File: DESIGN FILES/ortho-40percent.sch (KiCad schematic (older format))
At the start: 28 parts, among them J1 USB-C_Receptacle-24, SW1 SW_NO_4-Pin, U1 U_TPD4E05U06DQAR, U2 U_ATmega32u4-MU, Y1 XTAL_4Lead

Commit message: Consolidating design files
Added directory to store design separate from production files
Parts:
- removed C1, C2: C, ortho-40percent:C_0805, symbol master-vampire_General:C
- added C1, C2: C, master-vampire:C_0805, symbol master-vampire:C
- J1: symbol master-vampire_General:USB-C_Receptacle-24 -> master-vampire:USB-C_Receptacle-24
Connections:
- wire segments 171 -> 175
- no-connect marks 10 -> 13
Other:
- note added: "B"
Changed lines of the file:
@@
 $EndDescr
 $Comp
-L master-vampire_General:USB-C_Receptacle-24 J1
+L master-vampire:USB-C_Receptacle-24 J1
 U 1 1 5F1E69AB
 P 1450 2200
@@
 $EndComp
 $Comp
-L master-vampire_General:C C1
-U 1 1 5F248795
-P 5900 3650
-F 0 "C1" H 6015 3703 50  0000 L CNN
-F 1 "C" H 5900 3900 50  0001 L CNN
-F 2 "ortho-40percent:C_0805" H 5300 3450 50  0001 C CNN
-F 3 "" H 6050 3750 50  0000 C CNN
-F 4 "22pF" H 6015 3604 60  0000 L CNN "Capacitance"
-F 5 "50V" H 6400 3550 60  0001 C CNN "Voltage Rating"
-F 6 "C0G/NP0" H 6200 3500 60  0000 C CNN "TempCo"
-F 7 "±5%" H 6450 3650 60  0001 C CNN "Tolerance"
-F 8 "0805" H 6150 3450 60  0001 C CNN "Package"
-F 9 "C0805C220J5GACTU" H 5950 4000 50  0001 C CNN "MPN"
-F 10 "KEMET" H 6050 4100 50  0001 C CNN "Manufacturer"
-F 11 "DigiKey" H 6150 4200 50  0001 C CNN "Supplier"
-F 12 "399-1113-1-ND" H 6250 4300 50  0001 C CNN "Supplier PN"
-	1    5900 3650
-	1    0    0    -1
-$EndComp
-$Comp
-L master-vampire_General:C C2
-U 1 1 5F24AB6E
-P 6500 3650
-F 0 "C2" H 6615 3703 50  0000 L CNN
-F 1 "C" H 6500 3900 50  0001 L CNN
-F 2 "ortho-40percent:C_0805" H 5900 3450 50  0001 C CNN
-F 3 "" H 6650 3750 50  0000 C CNN
-F 4 "22pF" H 6615 3604 60  0000 L CNN "Capacitance"
-F 5 "50V" H 7000 3550 60  0001 C CNN "Voltage Rating"
-F 6 "C0G/NP0" H 6800 3500 60  0000 C CNN "TempCo"
-F 7 "±5%" H 7050 3650 60  0001 C CNN "Tolerance"
-F 8 "0805" H 6750 3450 60  0001 C CNN "Package"
-F 9 "C0805C220J5GACTU" H 6550 4000 50  0001 C CNN "MPN"
-F 10 "KEMET" H 6650 4100 50  0001 C CNN "Manufacturer"
-F 11 "DigiKey" H 6750 4200 50  0001 C CNN "Supplier"
-F 12 "399-1113-1-ND" H 6850 4300 50  0001 C CNN "Supplier PN"
-	1    6500 3650
-	1    0    0    -1
-$EndComp
-$Comp
 L power:VCC #PWR019
 U 1 1 5F24EA68
@@
 Wire Wire Line
 	6000 3300 5900 3300
-Wire Wire Line
-	5900 3300 5900 3500
-Wire Wire Line
-	6400 3300 6500 3300
-Wire Wire Line
-	6500 3300 6500 3500
 $Comp
 L power:GND #PWR013
 U 1 1 5F25E8F0
-P 5900 3900
-F 0 "#PWR013" H 5900 3650 50  0001 C CNN
-F 1 "GND" H 5900 3775 25  0000 C CNN
-F 2 "" H 5900 3900 50  0001 C CNN
-F 3 "" H 5900 3900 50  0001 C CNN
-	1    5900 3900
+P 5900 4100
+F 0 "#PWR013" H 5900 3850 50  0001 C CNN
+F 1 "GND" H 5900 3975 25  0000 C CNN
+F 2 "" H 5900 4100 50  0001 C CNN
+F 3 "" H 5900 4100 50  0001 C CNN
+	1    5900 4100
 	1    0    0    -1
 $EndComp
@@
 L power:GND #PWR015
 U 1 1 5F25EB3D
-P 6500 3900
-F 0 "#PWR015" H 6500 3650 50  0001 C CNN
-F 1 "GND" H 6500 3775 25  0000 C CNN
-F 2 "" H 6500 3900 50  0001 C CNN
-F 3 "" H 6500 3900 50  0001 C CNN
-	1    6500 3900
-	1    0    0    -1
-$EndComp
-Wire Wire Line
-	6500 3900 6500 3800
-Wire Wire Line
-	5900 3900 5900 3800
+P 6500 4100
+F 0 "#PWR015" H 6500 3850 50  0001 C CNN
+F 1 "GND" H 6500 3975 25  0000 C CNN
+F 2 "" H 6500 4100 50  0001 C CNN
+F 3 "" H 6500 4100 50  0001 C CNN
+	1    6500 4100
+	1    0    0    -1
+$EndComp
+Wire Wire Line
+	6500 4100 6500 4000
+Wire Wire Line
+	5900 4100 5900 4000
 $Comp
 L power:GND #PWR014
@@
 $EndComp
 Wire Wire Line
-	8600 3300 6500 3300
-Connection ~ 6500 3300
-Wire Wire Line
 	5900 3100 5900 3300
-Connection ~ 5900 3300
 $Comp
 L master-vampire_General:CP_tantalum C3
@@
 	7400 1500 7400 1350
 Wire Wire Line
-	7400 1050 7400 900
+	7400 1050 7400 1000
 $Sheet
 S 5000 5000 1550 1200
@@
 $EndComp
 Wire Wire Line
-	1200 3650 1200 3550
+	1200 3650 1200 3600
 Wire Wire Line
 	1300 3550 1300 3600
@@
 NoConn ~ 10000 3200
 NoConn ~ 10000 3600
+Text Notes 10600 7650 0    75   Italic 15
+B
+NoConn ~ 10000 4700
+NoConn ~ 10000 4800
+NoConn ~ 10000 4900
+$Comp
+L power:PWR_FLAG #FLG0102
+U 1 1 621A0DF7
+P 850 3600
+F 0 "#FLG0102" H 850 3675 50  0001 C CNN
+F 1 "PWR_FLAG" H 850 3773 50  0000 C CNN
+F 2 "" H 850 3600 50  0001 C CNN
+F 3 "~" H 850 3600 50  0001 C CNN
+	1    850  3600
+	-1   0    0    1
+$EndComp
+Wire Wire Line
+	850  3600 1200 3600
+Connection ~ 1200 3600
+Wire Wire Line
+	1200 3600 1200 3550
+$Comp
+L power:PWR_FLAG #FLG0103
+U 1 1 621B2AAF
+P 7100 1000
+F 0 "#FLG0103" H 7100 1075 50  0001 C CNN
+F 1 "PWR_FLAG" H 7100 1173 50  0000 C CNN
+F 2 "" H 7100 1000 50  0001 C CNN
+F 3 "~" H 7100 1000 50  0001 C CNN
+	1    7100 1000
+	1    0    0    -1
+$EndComp
+Wire Wire Line
+	7100 1000 7400 1000
+Connection ~ 7400 1000
+Wire Wire Line
+	7400 1000 7400 900
+$Comp
+L master-vampire:C C1
+U 1 1 621BCCD9
+P 5900 3850
+F 0 "C1" H 6015 4002 50  0000 L CNN
+F 1 "C" H 5900 4100 50  0001 L CNN
+F 2 "master-vampire:C_0805" H 5300 3650 50  0001 C CNN
+F 3 "" H 6050 3950 50  0000 C CNN
+F 4 "22pF" H 6015 3903 60  0000 L CNN "Capacitance"
+F 5 "50V" H 6400 3750 60  0001 C CNN "Voltage Rating"
+F 6 "C0G/NP0" H 6015 3797 60  0000 L CNN "TempCo"
+F 7 "5per" H 6450 3850 60  0001 C CNN "Tolerance"
+F 8 "0805" H 6150 3650 60  0001 C CNN "Package"
+F 9 "C0805C220J5GACTU" H 5950 4200 50  0001 C CNN "MPN"
+F 10 "KEMET" H 6050 4300 50  0001 C CNN "Manufacturer"
+F 11 "DigiKey" H 6150 4400 50  0001 C CNN "Supplier"
+F 12 "399-1113-1-ND" H 6250 4500 50  0001 C CNN "Supplier PN"
+F 13 "20000-A" H 6015 3699 50  0000 L CNN "MV PN"
+	1    5900 3850
+	1    0    0    -1
+$EndComp
+Wire Wire Line
+	5900 3300 5900 3700
+Connection ~ 5900 3300
+Wire Wire Line
+	6400 3300 6500 3300
+Wire Wire Line
+	6500 3300 6500 3700
+Connection ~ 6500 3300
+Wire Wire Line
+	6500 3300 8600 3300
+$Comp
+L master-vampire:C C2
+U 1 1 621E57A6
+P 6500 3850
+F 0 "C2" H 6615 4002 50  0000 L CNN
+F 1 "C" H 6500 4100 50  0001 L CNN
+F 2 "master-vampire:C_0805" H 6615 3956 50  0001 L CNN
+F 3 "" H 6650 3950 50  0000 C CNN
+F 4 "22pF" H 6615 3903 60  0000 L CNN "Capacitance"
+F 5 "50V" H 7000 3750 60  0001 C CNN "Voltage Rating"
+F 6 "C0G/NP0" H 6615 3797 60  0000 L CNN "TempCo"
+F 7 "5per" H 7050 3850 60  0001 C CNN "Tolerance"
+F 8 "0805" H 6750 3650 60  0001 C CNN "Package"
+F 9 "C0805C220J5GACTU" H 6550 4200 50  0001 C CNN "MPN"
+F 10 "KEMET" H 6650 4300 50  0001 C CNN "Manufacturer"
+F 11 "DigiKey" H 6750 4400 50  0001 C CNN "Supplier"
+F 12 "399-1113-1-ND" H 6850 4500 50  0001 C CNN "Supplier PN"
+F 13 "20000-A" H 6615 3699 50  0000 L CNN "MV PN"
+	1    6500 3850
+	1    0    0    -1
+$EndComp
 $EndSCHEMATC

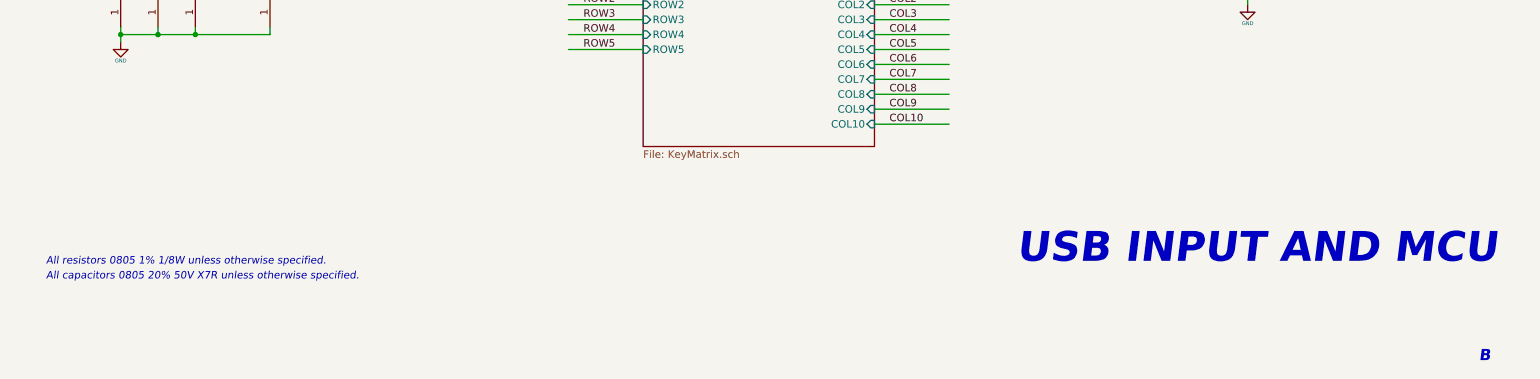
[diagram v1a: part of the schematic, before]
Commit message: Added stencil guide holes
Added 2.6mm dia guide holes at 10mm spacings to board to help with stencil alignment
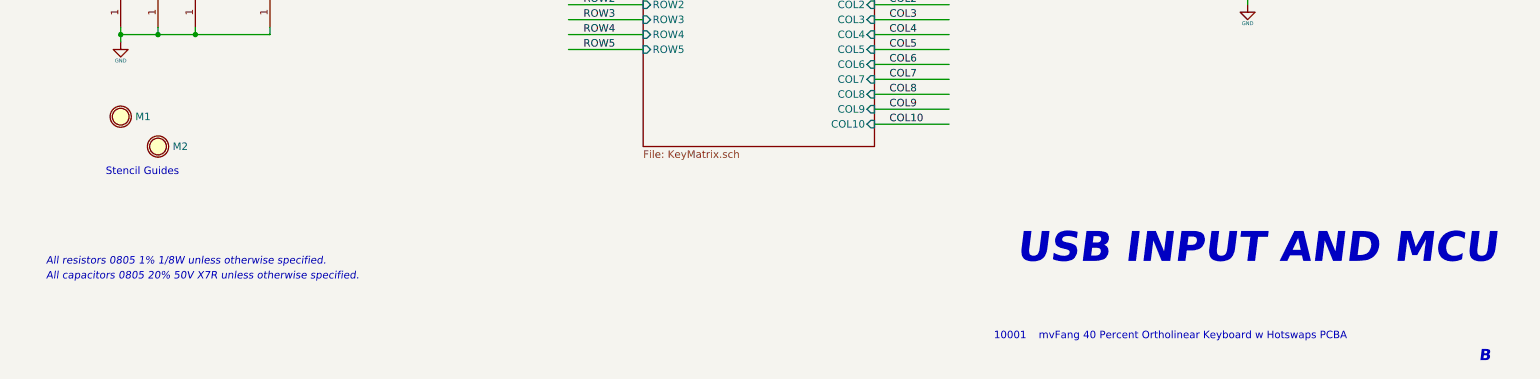
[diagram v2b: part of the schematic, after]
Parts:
- added M1, M2: M_StencilGuide, master-vampire:STENCIL_GUIDE_HOLE, symbol master-vampire:M_StencilGuide
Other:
- note added: "10001"
- note added: "Stencil Guides"
- note added: "mvFang 40 Percent Ortholinear Keyboard w Hotswaps PCBA"
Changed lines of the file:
@@
 	1    0    0    -1
 $EndComp
+Text Notes 7650 7500 0    50   ~ 0
+mvFang 40 Percent Ortholinear Keyboard w Hotswaps PCBA
+Text Notes 7350 7500 0    50   ~ 0
+10001
+$Comp
+L master-vampire:M_StencilGuide M1
+U 1 1 624BB73E
+P 1500 6000
+F 0 "M1" H 1598 6000 50  0000 L CNN
+F 1 "M_StencilGuide" H 1500 5850 50  0001 C CNN
+F 2 "master-vampire:STENCIL_GUIDE_HOLE" H 1500 5850 50  0001 C CNN
+F 3 "" H 1500 5850 50  0001 C CNN
+F 4 "DNP" H 1450 5850 50  0001 C CNN "Manufacturer"
+F 5 "DNP" H 1500 5850 50  0001 C CNN "MPN"
+F 6 "DNP" H 1500 5850 50  0001 C CNN "MV PN"
+	1    1500 6000
+	1    0    0    -1
+$EndComp
+$Comp
+L master-vampire:M_StencilGuide M2
+U 1 1 624BC60C
+P 1750 6200
+F 0 "M2" H 1848 6200 50  0000 L CNN
+F 1 "M_StencilGuide" H 1750 6050 50  0001 C CNN
+F 2 "master-vampire:STENCIL_GUIDE_HOLE" H 1750 6050 50  0001 C CNN
+F 3 "" H 1750 6050 50  0001 C CNN
+F 4 "DNP" H 1700 6050 50  0001 C CNN "Manufacturer"
+F 5 "DNP" H 1750 6050 50  0001 C CNN "MPN"
+F 6 "DNP" H 1750 6050 50  0001 C CNN "MV PN"
+	1    1750 6200
+	1    0    0    -1
+$EndComp
+Text Notes 1400 6400 0    50   ~ 0
+Stencil Guides
 $EndSCHEMATC

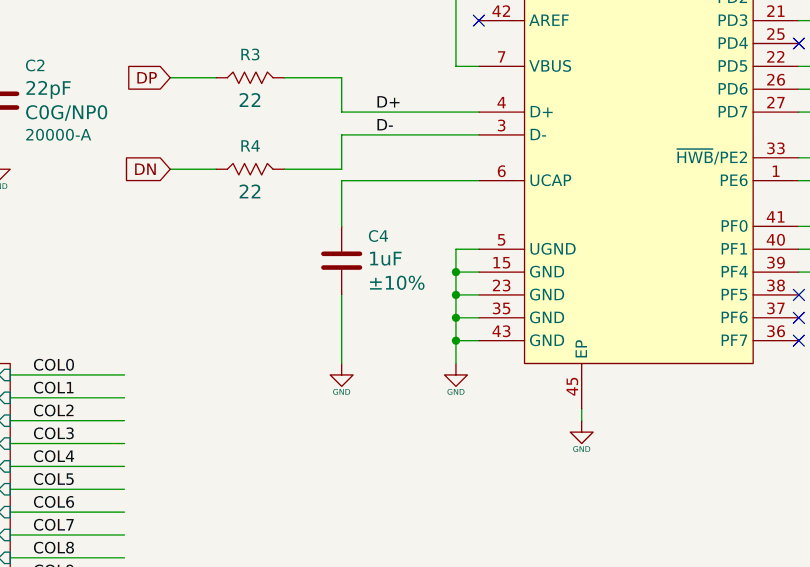
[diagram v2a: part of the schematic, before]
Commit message: Added custom MV PNs to each component
Added unique MV PN for each unique component, referenced in personal component database.
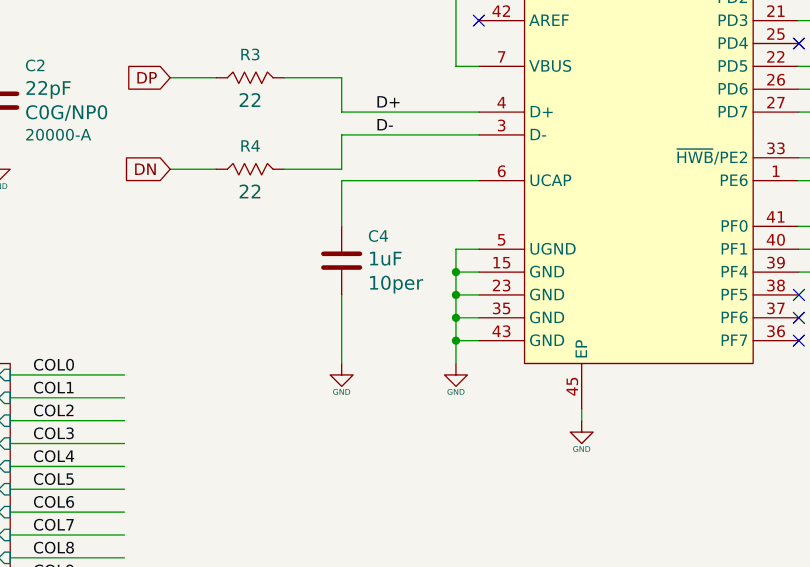
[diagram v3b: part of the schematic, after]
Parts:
- C3: MV PN (none) -> 20001-A; Tolerance ±20% -> 20per
- C4: MV PN (none) -> 20002-A; Tolerance ±10% -> 10per
- C5: MV PN (none) -> 20003-A; Tolerance ±20% -> 20per
- C6, C7, C8, C9: MV PN (none) -> 20003-A
- F1: MV PN (none) -> 20005-A
- H1, H2, H3, H4, H5: MV PN (none) -> DNP
- J1: MV PN (none) -> 20006-A
- L1: MV PN (none) -> 20007-A; Tolerance 20% -> 20per
- R1, R2: MV PN (none) -> 20008-A; Tolerance 1% -> 1per
- R3, R4: MV PN (none) -> 20009-A; Tolerance 1% -> 1per
- R5, R6: MV PN (none) -> 20010-A; Tolerance 1% -> 1per
- SW1: MV PN (none) -> 20011-A
- TVS1: MV PN (none) -> 20012-A
- U1: MV PN (none) -> 20013-A
- U2: MV PN (none) -> 20014-A
- Y1: MV PN (none) -> 20015-A
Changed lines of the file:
@@
 F 7 "12401598E4#2ACT-ND" H 1450 2200 50  0001 C CNN "Supplier PN"
 F 8 "Surface Mount, Right Angle; Through Hole" H 1450 2200 50  0001 C CNN "Package"
+F 9 "20006-A" H 1450 2200 50  0001 C CNN "MV PN"
 	1    1450 2200
 	1    0    0    -1
@@
 F 5 "1/8W" H 2350 1250 60  0001 C CNN "Power"
 F 6 "0805" H 2150 1250 60  0001 C CNN "Package"
-F 7 "1%" H 2400 1400 60  0001 C CNN "Tolerance"
+F 7 "1per" H 2400 1400 60  0001 C CNN "Tolerance"
 F 8 "ERJ-6ENF5101V" H 2750 2100 50  0001 C CNN "MPN"
 F 9 "Panasonic Electronic Components" H 2850 2200 50  0001 C CNN "Manufacturer"
 F 10 "DigiKey" H 2950 2300 50  0001 C CNN "Supplier"
 F 11 "P5.10KCCT-ND" H 3050 2400 50  0001 C CNN "Supplier PN"
+F 12 "20008-A" H 2250 1500 50  0001 C CNN "MV PN"
 	1    2250 1500
 	1    0    0    -1
@@
 F 5 "1/8W" H 2900 1450 60  0001 C CNN "Power"
 F 6 "0805" H 2700 1450 60  0001 C CNN "Package"
-F 7 "1%" H 2950 1600 60  0001 C CNN "Tolerance"
+F 7 "1per" H 2950 1600 60  0001 C CNN "Tolerance"
 F 8 "ERJ-6ENF5101V" H 3300 2300 50  0001 C CNN "MPN"
 F 9 "Panasonic Electronic Components" H 3400 2400 50  0001 C CNN "Manufacturer"
 F 10 "DigiKey" H 3500 2500 50  0001 C CNN "Supplier"
 F 11 "P5.10KCCT-ND" H 3600 2600 50  0001 C CNN "Supplier PN"
+F 12 "20008-A" H 2800 1700 50  0001 C CNN "MV PN"
 	1    2800 1700
 	1    0    0    -1
@@
 F 6 "4A" H 1900 4050 60  0001 C CNN "Current Rating"
 F 7 "10mOhm" H 2000 3900 60  0001 C CNN "DC Resistance"
-F 8 "20%" H 2200 4150 60  0001 C CNN "Tolerance"
+F 8 "20per" H 2200 4150 60  0001 C CNN "Tolerance"
 F 9 "FBMJ3216HM600-T" H 2600 4950 50  0001 C CNN "MPN"
 F 10 "Taiyo Yuden" H 2700 5050 50  0001 C CNN "Manufacturer"
 F 11 "DigiKey" H 2800 5150 50  0001 C CNN "Supplier"
 F 12 "587-1770-1-ND" H 2900 5250 50  0001 C CNN "Supplier PN"
+F 13 "20007-A" H 2000 4250 50  0001 C CNN "MV PN"
 	1    2000 4250
 	0    1    1    0
@@
 F 7 "DNP" H 4300 3100 50  0001 C CNN "Supplier PN"
 F 8 "UFDFN-10" H 4300 3100 50  0001 C CNN "Package"
+F 9 "20013-A" H 4300 3100 50  0001 C CNN "MV PN"
 	1    4300 3100
 	1    0    0    -1
@@
 F 8 "1206" H 4300 1250 50  0000 C CNN "Package"
 F 9 "500mA" H 4300 1150 50  0000 C CNN "Hold Current"
+F 10 "20005-A" H 4300 1400 50  0001 C CNN "MV PN"
 	1    4300 1400
 	1    0    0    -1
@@
 F 5 "50V" H 8500 4450 60  0001 C CNN "Voltage Rating"
 F 6 "X7R" H 8250 4450 60  0001 C CNN "TempCo"
-F 7 "±10%" H 8115 4451 60  0000 L CNN "Tolerance"
+F 7 "10per" H 8115 4451 60  0000 L CNN "Tolerance"
 F 8 "0805" H 8250 4350 60  0001 C CNN "Package"
 F 9 "CL21B105KBFNNNG" H 8050 4900 50  0001 C CNN "MPN"
@@
 F 11 "DigiKey" H 8250 5100 50  0001 C CNN "Supplier"
 F 12 "1276-6470-1-ND" H 8350 5200 50  0001 C CNN "Supplier PN"
+F 13 "20002-A" H 8000 4550 50  0001 C CNN "MV PN"
 	1    8000 4550
 	1    0    0    -1
@@
 F 5 "1/8W" H 7700 3950 60  0001 C CNN "Power"
 F 6 "0805" H 7800 3950 60  0001 C CNN "Package"
-F 7 "1%" H 7750 4050 60  0001 C CNN "Tolerance"
+F 7 "1per" H 7750 4050 60  0001 C CNN "Tolerance"
 F 8 "RC0805FR-0722RL" H 8100 4750 50  0001 C CNN "MPN"
 F 9 "Yageo" H 8200 4850 50  0001 C CNN "Manufacturer"
 F 10 "Digikey" H 8300 4950 50  0001 C CNN "Supplier"
 F 11 "311-22.0CRCT-ND" H 8400 5050 50  0001 C CNN "Supplier PN"
+F 12 "20009-A" H 7600 4150 50  0001 C CNN "MV PN"
 	1    7600 4150
 	1    0    0    -1
@@
 F 5 "1/8W" H 7700 3550 60  0001 C CNN "Power"
 F 6 "0805" H 7800 3550 60  0001 C CNN "Package"
-F 7 "1%" H 7750 3650 60  0001 C CNN "Tolerance"
+F 7 "1per" H 7750 3650 60  0001 C CNN "Tolerance"
 F 8 "RC0805FR-0722RL" H 8100 4350 50  0001 C CNN "MPN"
 F 9 "Yageo" H 8200 4450 50  0001 C CNN "Manufacturer"
 F 10 "Digikey" H 8300 4550 50  0001 C CNN "Supplier"
 F 11 "311-22.0CRCT-ND" H 8400 4650 50  0001 C CNN "Supplier PN"
+F 12 "20009-A" H 7600 3750 50  0001 C CNN "MV PN"
 	1    7600 3750
 	1    0    0    -1
@@
 F 5 "1/8W" H 11050 4350 60  0001 C CNN "Power"
 F 6 "0805" H 10700 4350 60  0001 C CNN "Package"
-F 7 "1%" H 10950 4450 60  0001 C CNN "Tolerance"
+F 7 "1per" H 10950 4450 60  0001 C CNN "Tolerance"
 F 8 "RC0805FR-0710KL" H 11150 5150 50  0001 C CNN "MPN"
 F 9 "Yageo" H 11250 5250 50  0001 C CNN "Manufacturer"
 F 10 "DigiKey" H 11350 5350 50  0001 C CNN "Supplier"
 F 11 "311-10.0KCRCT-ND" H 11450 5450 50  0001 C CNN "Supplier PN"
+F 12 "20010-A" H 10650 4550 50  0001 C CNN "MV PN"
 	1    10650 4550
 	0    1    1    0
@@
 F 11 "DigiKey" H 9050 1750 50  0001 C CNN "Supplier"
 F 12 "399-1169-1-ND" H 9150 1850 50  0001 C CNN "Supplier PN"
+F 13 "20003-A" H 8800 1200 50  0001 C CNN "MV PN"
 	1    8800 1200
 	1    0    0    -1
@@
 F 5 "1/8W" H 8400 2350 60  0001 C CNN "Power"
 F 6 "0805" H 8050 2350 60  0001 C CNN "Package"
-F 7 "1%" H 8300 2450 60  0001 C CNN "Tolerance"
+F 7 "1per" H 8300 2450 60  0001 C CNN "Tolerance"
 F 8 "RC0805FR-0710KL" H 8500 3150 50  0001 C CNN "MPN"
 F 9 "Yageo" H 8600 3250 50  0001 C CNN "Manufacturer"
 F 10 "DigiKey" H 8700 3350 50  0001 C CNN "Supplier"
 F 11 "311-10.0KCRCT-ND" H 8800 3450 50  0001 C CNN "Supplier PN"
+F 12 "20010-A" H 8000 2550 50  0001 C CNN "MV PN"
 	1    8000 2550
 	0    1    1    0
@@
 F 8 "DigiKey" H 6810 4130 50  0001 C CNN "Supplier"
 F 9 "1253-1698-1-ND" H 6910 4230 50  0001 C CNN "Supplier PN"
+F 10 "20015-A" H 6200 3300 50  0001 C CNN "MV PN"
 	1    6200 3300
 	1    0    0    -1
@@
 F 11 "DigiKey" H 9550 1750 50  0001 C CNN "Supplier"
 F 12 "399-1169-1-ND" H 9650 1850 50  0001 C CNN "Supplier PN"
+F 13 "20003-A" H 9300 1200 50  0001 C CNN "MV PN"
 	1    9300 1200
 	1    0    0    -1
@@
 F 11 "DigiKey" H 10050 1750 50  0001 C CNN "Supplier"
 F 12 "399-1169-1-ND" H 10150 1850 50  0001 C CNN "Supplier PN"
+F 13 "20003-A" H 9800 1200 50  0001 C CNN "MV PN"
 	1    9800 1200
 	1    0    0    -1
@@
 F 11 "DigiKey" H 10550 1750 50  0001 C CNN "Supplier"
 F 12 "399-1169-1-ND" H 10650 1850 50  0001 C CNN "Supplier PN"
+F 13 "20003-A" H 10300 1200 50  0001 C CNN "MV PN"
 	1    10300 1200
 	1    0    0    -1
@@
 F 7 "C&K" H 8050 3510 50  0001 C CNN "Manufacturer"
 F 8 "Surface Mount" H 8150 3610 50  0001 C CNN "Package"
+F 9 "20011-A" H 7300 2800 50  0001 C CNN "MV PN"
 	1    7300 2800
 	1    0    0    -1
@@
 F 5 "50V" H 8650 1100 60  0001 C CNN "Voltage Rating"
 F 6 "X7R" H 8400 1100 60  0001 C CNN "TempCo"
-F 7 "±20%" H 8700 1200 60  0001 C CNN "Tolerance"
+F 7 "20per" H 8700 1200 60  0001 C CNN "Tolerance"
 F 8 "0805" H 8400 1000 60  0001 C CNN "Package"
 F 9 "C0805C104M5RACTU" H 8200 1550 50  0001 C CNN "MPN"
@@
 F 11 "DigiKey" H 8400 1750 50  0001 C CNN "Supplier"
 F 12 "399-1169-1-ND" H 8500 1850 50  0001 C CNN "Supplier PN"
+F 13 "20003-A" H 8150 1200 50  0001 C CNN "MV PN"
 	1    8150 1200
 	1    0    0    -1
@@
 F 5 "10V" H 7510 1207 60  0000 L CNN "Voltage Rating"
 F 6 "Tantalum" H 7510 1101 60  0000 L CNN "TempCo"
-F 7 "±20%" H 7950 1200 60  0001 C CNN "Tolerance"
+F 7 "20per" H 7950 1200 60  0001 C CNN "Tolerance"
 F 8 "1206" H 7510 995 60  0000 L CNN "Package"
 F 9 "T520A106M010ATE080" H 7450 1550 50  0001 C CNN "MPN"
@@
 F 11 "DigiKey" H 7650 1750 50  0001 C CNN "Supplier"
 F 12 "399-4788-1-ND" H 7750 1850 50  0001 C CNN "Supplier PN"
+F 13 "20001-A" H 7400 1200 50  0001 C CNN "MV PN"
 	1    7400 1200
 	1    0    0    -1
@@
 F 7 "DNP" H 1900 5600 50  0001 C CNN "Supplier"
 F 8 "DNP" H 2000 5700 50  0001 C CNN "Package"
+F 9 "DNP" H 1500 5100 50  0001 C CNN "MV PN"
 	1    1500 5100
 	0    -1   -1   0
@@
 F 7 "DNP" H 2150 5600 50  0001 C CNN "Supplier"
 F 8 "DNP" H 2250 5700 50  0001 C CNN "Package"
+F 9 "DNP" H 1750 5100 50  0001 C CNN "MV PN"
 	1    1750 5100
 	0    -1   -1   0
@@
 F 7 "DNP" H 2400 5600 50  0001 C CNN "Supplier"
 F 8 "DNP" H 2500 5700 50  0001 C CNN "Package"
+F 9 "DNP" H 2000 5100 50  0001 C CNN "MV PN"
 	1    2000 5100
 	0    -1   -1   0
@@
 F 7 "DNP" H 1900 4600 50  0001 C CNN "Supplier"
 F 8 "DNP" H 2000 4700 50  0001 C CNN "Package"
+F 9 "DNP" H 1500 4100 50  0001 C CNN "MV PN"
 	1    1500 4100
 	0    -1   -1   0
@@
 F 7 "DNP" H 2900 5600 50  0001 C CNN "Supplier"
 F 8 "DNP" H 3000 5700 50  0001 C CNN "Package"
+F 9 "DNP" H 2500 5100 50  0001 C CNN "MV PN"
 	1    2500 5100
 	0    -1   -1   0
@@
 F 7 "DigiKey" H 5150 2400 50  0001 C CNN "Supplier"
 F 8 "SOD-123F" H 5250 2500 50  0001 C CNN "Package"
+F 9 "20012-A" H 4600 1650 50  0001 C CNN "MV PN"
 	1    4600 1650
 	0    1    1    0
@@
 F 7 "ATMEGA32U4-MU-ND" H 9200 3400 50  0001 C CNN "Supplier PN"
 F 8 "VQFN-44-1EP" H 9200 3400 50  0001 C CNN "Package"
+F 9 "20014-A" H 9300 3500 50  0001 C CNN "MV PN"
 	1    9300 3500
 	1    0    0    -1
